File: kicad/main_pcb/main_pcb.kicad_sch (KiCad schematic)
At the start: 30 parts, among them J1 BAT_PWR, J2 LCD_I2C, J3 ECT_EXT, J4 EOT, J5 EOP, K2 3570.1331.051, Q1 PN2222A

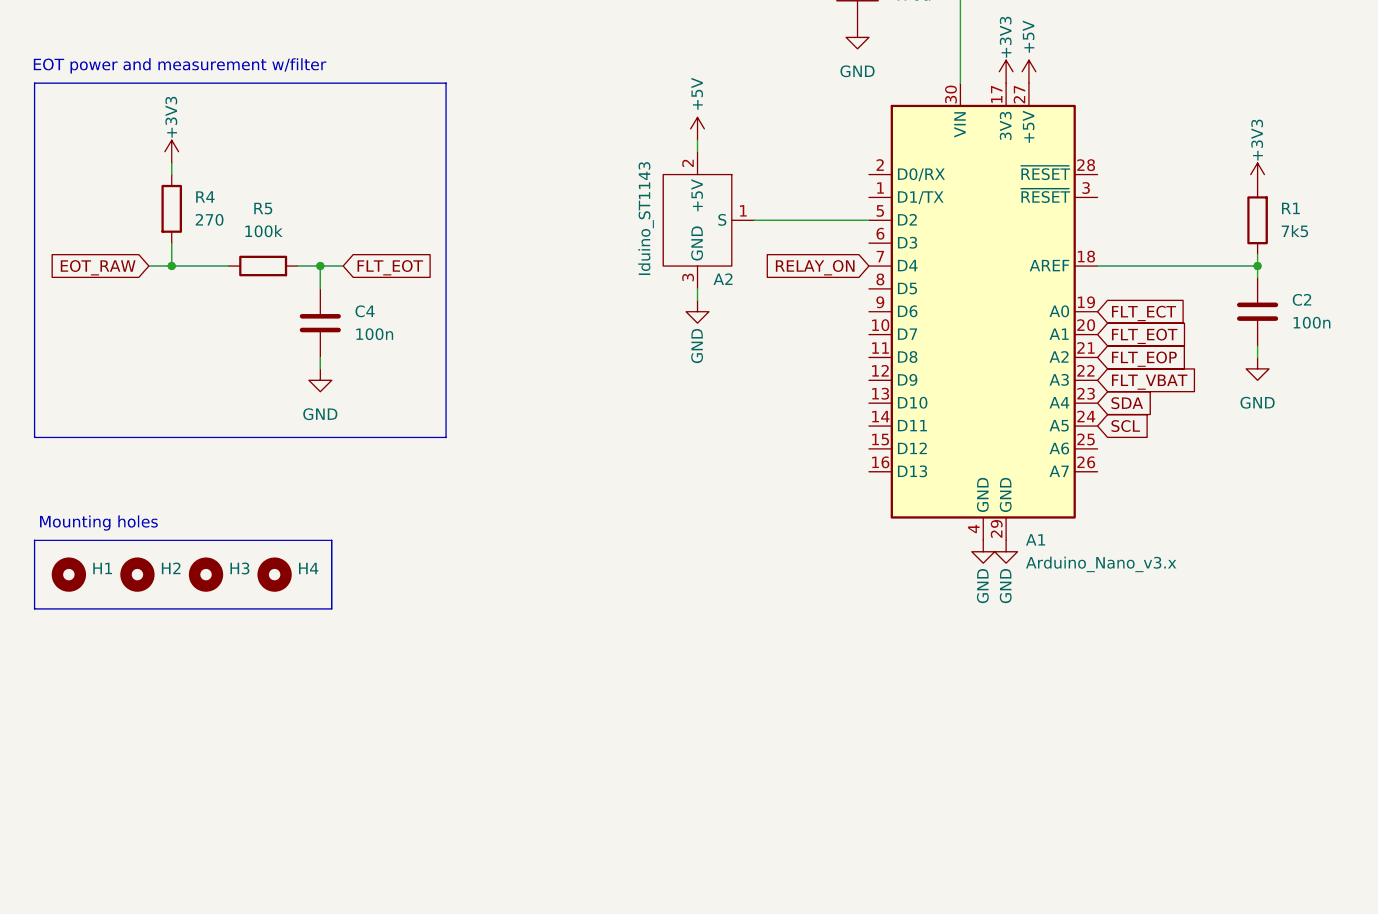
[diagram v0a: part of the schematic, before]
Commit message: Main PCB final design, refine eot calibration and limits
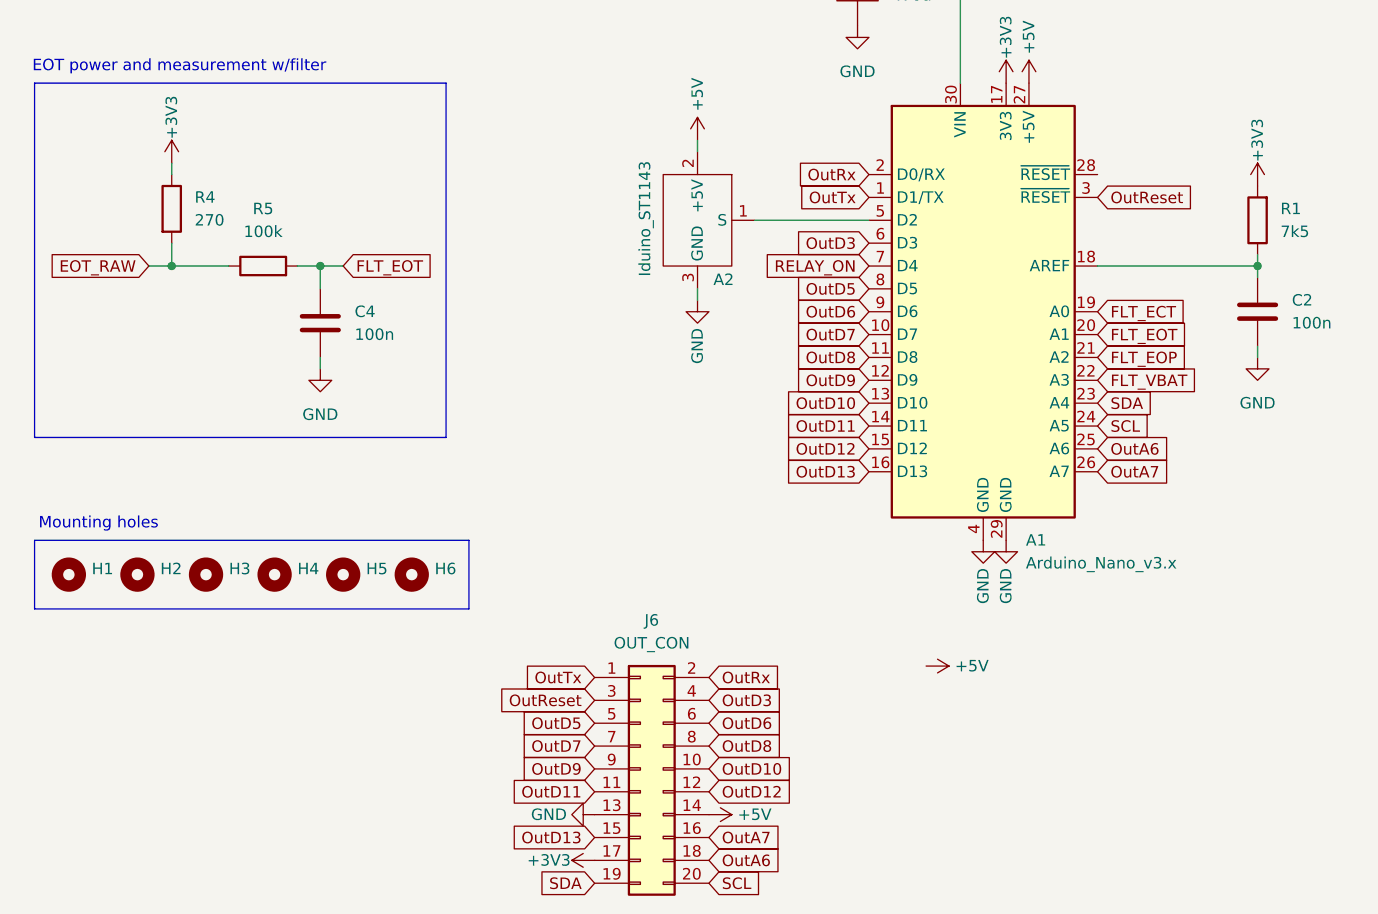
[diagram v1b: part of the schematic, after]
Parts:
- added H5, H6: ~, MountingHole:MountingHole_3.5mm, symbol Mechanical:MountingHole
- added J6: OUT_CON, Connector_IDC:IDC-Header_2x10_P2.54mm_Vertical, symbol Connector_Generic:Conn_02x10_Odd_Even
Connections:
- net +3V3: now also J6.17 (Pin_17)
- net +5V: now also J6.14 (Pin_14)
- net GND: now also J6.13 (Pin_13)
- net SCL: now also J6.20 (Pin_20)
- net SDA: now also J6.19 (Pin_19)
- net OutTx: now reaches A1.1 (D1/TX)
- net OutTx: now also J6.1 (Pin_1)
- net OutD7: now reaches A1.10 (D7)
- net OutD7: now also J6.7 (Pin_7)
- net OutD8: now reaches A1.11 (D8)
- net OutD8: now also J6.8 (Pin_8)
- net OutD9: now reaches A1.12 (D9)
- net OutD9: now also J6.9 (Pin_9)
- net OutD10: now reaches A1.13 (D10)
- net OutD10: now also J6.10 (Pin_10)
- net OutD11: now reaches A1.14 (D11)
- net OutD11: now also J6.11 (Pin_11)
- net OutD12: now reaches A1.15 (D12)
- net OutD12: now also J6.12 (Pin_12)
- net OutD13: now reaches A1.16 (D13)
- net OutD13: now also J6.15 (Pin_15)
- net OutRx: now reaches A1.2 (D0/RX)
- net OutRx: now also J6.2 (Pin_2)
- net OutA6: now reaches A1.25 (A6)
- net OutA6: now also J6.18 (Pin_18)
- net OutA7: now reaches A1.26 (A7)
- net OutA7: now also J6.16 (Pin_16)
- net OutReset: now reaches A1.3 (~{RESET})
- net OutReset: now also J6.3 (Pin_3)
- net OutD3: now reaches A1.6 (D3)
- net OutD3: now also J6.4 (Pin_4)
- net OutD5: now reaches A1.8 (D5)
- net OutD5: now also J6.5 (Pin_5)
- net OutD6: now reaches A1.9 (D6)
- net OutD6: now also J6.6 (Pin_6)

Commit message: Component adjustments and recalibration
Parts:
- R1: value 7k5 -> 6k8
- R7: value 33k -> 47k
- R8: value 5k -> 6k8
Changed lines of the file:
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@@
 			)
 		)
-		(property "Value" "7k5"
+		(property "Value" "6k8"
 			(at 171.45 91.4399 0)
 			(effects
@@
 			)
 		)
-		(property "Value" "5k"
+		(property "Value" "6k8"
 			(at 215.9 128.2699 0)
 			(effects
@@
 			)
 		)
-		(property "Value" "33k"
+		(property "Value" "47k"
 			(at 215.9 115.5699 0)
 			(effects
